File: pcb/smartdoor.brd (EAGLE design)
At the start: 40.3 x 53.3 mm, 5 parts

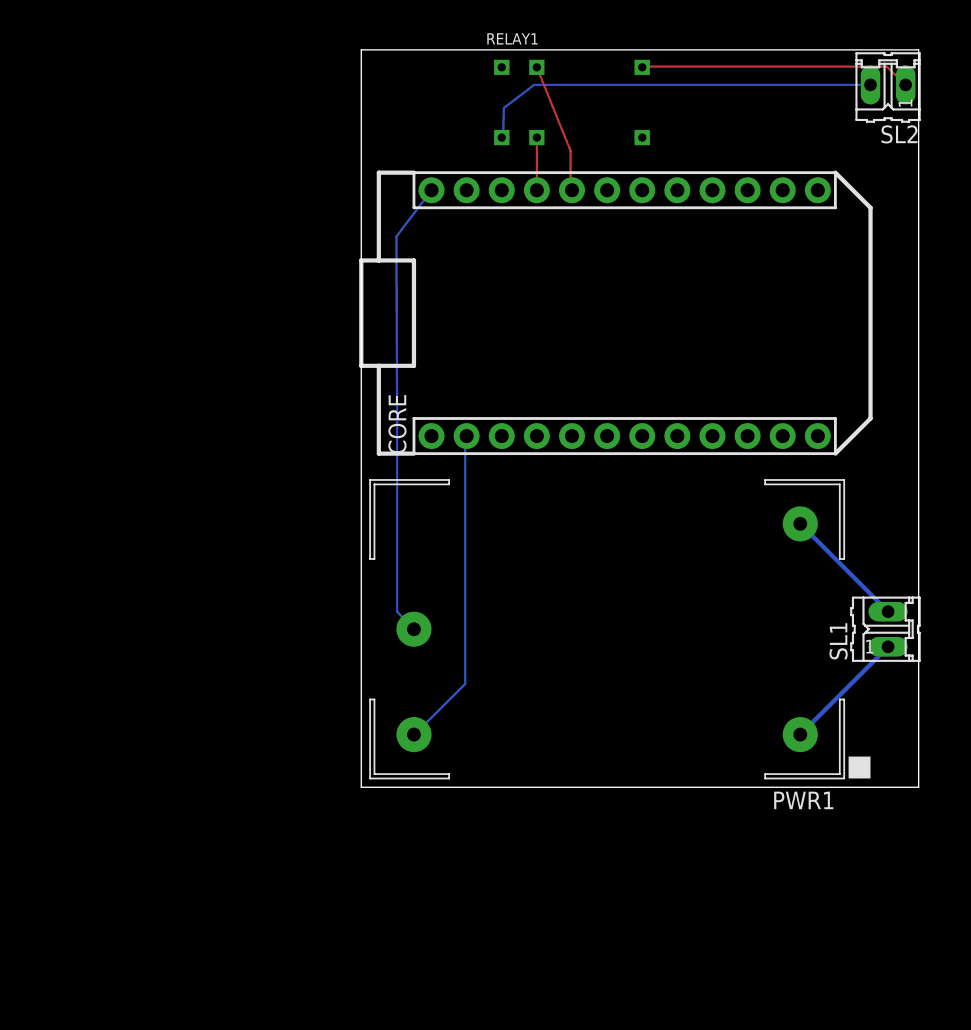
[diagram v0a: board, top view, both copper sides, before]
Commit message: new pcb board layout, renamed files
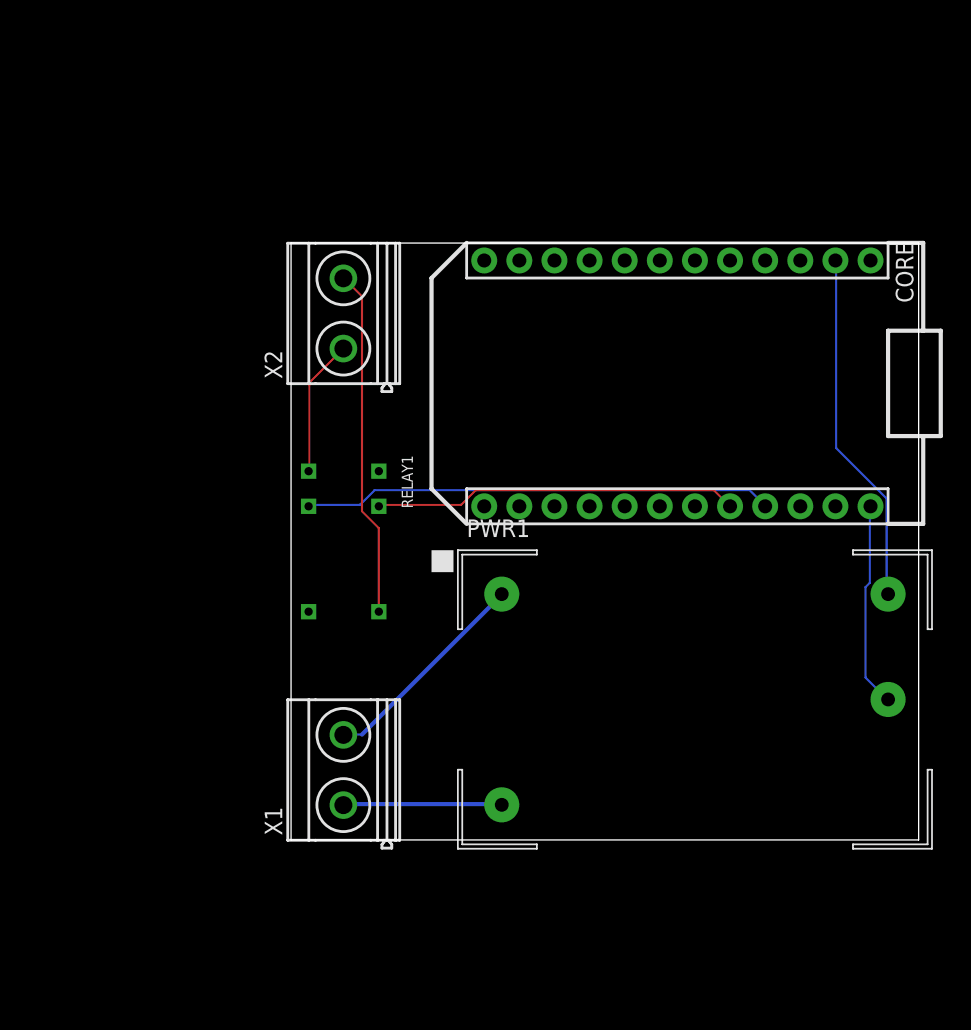
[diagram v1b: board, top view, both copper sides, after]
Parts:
- removed SL1, SL2: (no value), con-amp-quick:02P
- added X1, X2: MKDSN1,5/2-5,08, con-phoenix-508:MKDSN1,5/2-5,08
- moved RELAY1 35.8 mm to (20.3, 33.0), turned to 270 degrees
- moved PWR1 6.35 mm to (44.5, 21.6), turned to 0 degrees
- moved CORE 6.35 mm to (44.5, 44.5), turned to 270 degrees
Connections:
- net L: now also X1.1; no longer SL1.2
- net LOAD+: now also X2.2; no longer SL2.1
- net LOAD-: now also X2.1; no longer SL2.2
- net N: now also X1.2; no longer SL1.1
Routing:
- net GND2: track 3.81 -> 34.0 mm
- net LOAD-: track 29.3 -> 9.94 mm
- net 3V3: track 33.1 -> 14.8 mm
- net SWITCH: track 9.41 -> 26.4 mm
- net N: track 8.98 -> 15.7 mm
- net LOAD+: track 19.6 -> 25.2 mm
- net GND: track 23.2 -> 25.8 mm
- net L: track 8.98 -> 11.5 mm
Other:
- board size 40.3 x 53.3 mm -> 45.4 x 43.2 mm

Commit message: defined net classes and GND pins on relay, new board layout
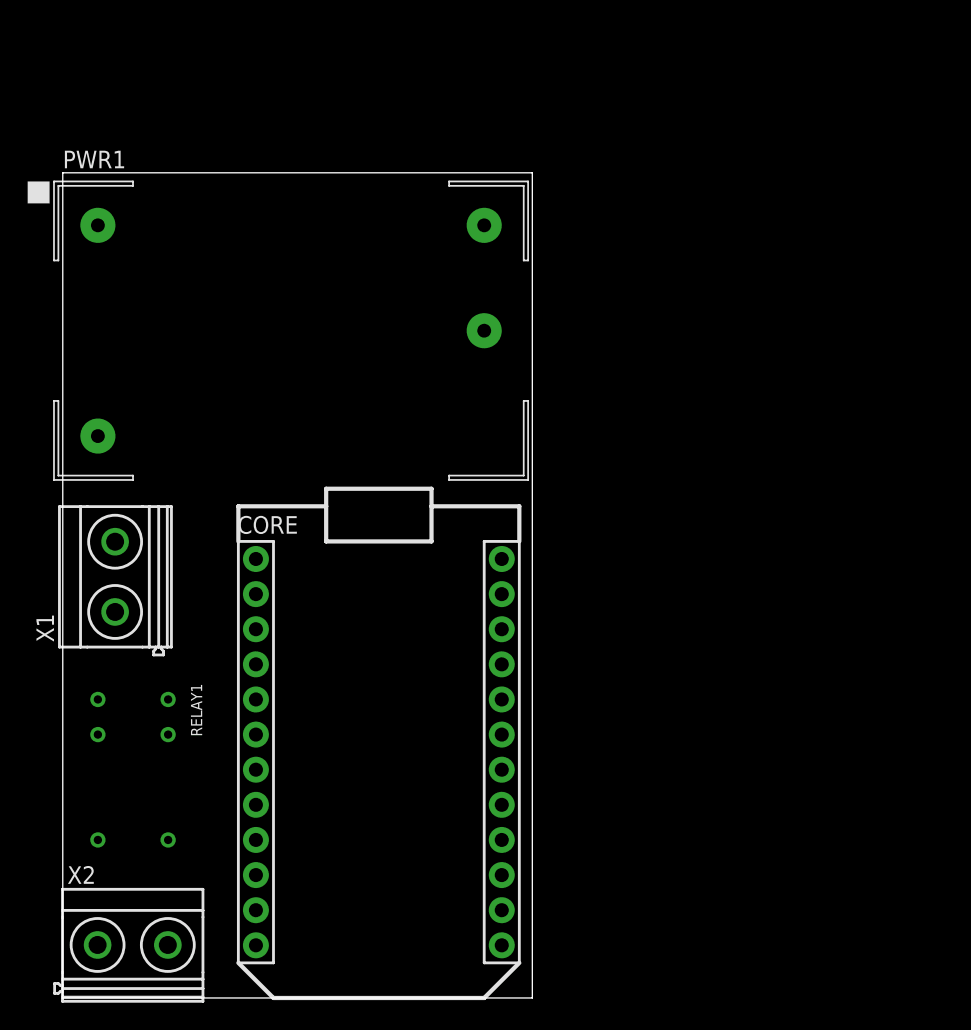
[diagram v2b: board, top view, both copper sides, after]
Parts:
- moved X2 48.2 mm to (5.08, 3.81), turned to 0 degrees
- moved PWR1 39.6 mm to (15.2, 48.3)
- moved CORE 34.3 mm to (22.9, 17.8), turned to 0 degrees
- moved RELAY1 22.5 mm to (5.08, 16.5)
- moved X1 21.6 mm to (3.81, 30.5)
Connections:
- removed net GND2: CORE.21, RELAY1.9
- new net N$1: CORE.2, PWR1.P3
- net GND: now also CORE.21, RELAY1.9; no longer CORE.2, PWR1.P3
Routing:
- net GND2: track 34.0 -> 0.00 mm
- net SWITCH: track 26.4 -> 0.00 mm
- net GND: track 25.8 -> 0.00 mm
- net LOAD+: track 25.2 -> 0.00 mm
- net N: track 15.7 -> 0.00 mm
- net 3V3: track 14.8 -> 0.00 mm
- net L: track 11.5 -> 0.00 mm
- net LOAD-: track 9.94 -> 0.00 mm
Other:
- board size 45.4 x 43.2 mm -> 34 x 59.7 mm
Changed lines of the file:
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@@
 <board>
 <plain>
-<wire x1="16.51" y1="11.43" x2="61.9" y2="11.43" width="0" layer="20"/>
-<wire x1="61.9" y1="11.43" x2="61.9" y2="54.6" width="0" layer="20"/>
-<wire x1="61.9" y1="54.6" x2="16.51" y2="54.6" width="0" layer="20"/>
-<wire x1="16.51" y1="54.6" x2="16.51" y2="11.43" width="0" layer="20"/>
+<wire x1="0" y1="0" x2="33.96" y2="0" width="0" layer="20"/>
+<wire x1="33.96" y1="0" x2="33.96" y2="59.68" width="0" layer="20"/>
+<wire x1="33.96" y1="59.68" x2="0" y2="59.68" width="0" layer="20"/>
+<wire x1="0" y1="59.68" x2="0" y2="0" width="0" layer="20"/>
 </plain>
 <attributes>
@@
 </variantdefs>
 <classes>
-<class number="0" name="default" width="0" drill="0">
+<class number="0" name="default" width="0.6096" drill="0.6096">
+<clearance class="0" value="0.6096"/>
 </class>
 </classes>
@@
 <param name="RoutingGrid" value="50mil"/>
 <param name="AutoGrid" value="1"/>
-<param name="Efforts" value="2"/>
+<param name="Efforts" value="0"/>
 <param name="TopRouterVariant" value="1"/>
 <param name="tpViaShape" value="round"/>
@@
 </autorouter>
 <elements>
-<element name="CORE" library="Particle" package="SPARK_CORE" value="SPARK_CORECORE" x="44.45" y="44.45" rot="R270"/>
-<element name="PWR1" library="recom-powerline-acdc-converters" package="LOW_PROFILE_POWER_MODULE" value="RAC02-3.3SC" x="44.45" y="21.59">
-<attribute name="INPUT_RANGE" value="80 - 277 (VAC)" x="44.45" y="21.59" size="1.778" layer="27" display="off"/>
-<attribute name="MAX_CAPACITIVE_LOAD" value="2000uF" x="44.45" y="21.59" size="1.778" layer="27" display="off"/>
-<attribute name="OUTPUT_CURRENT" value="600mA" x="44.45" y="21.59" size="1.778" layer="27" display="off"/>
-<attribute name="OUTPUT_VOLTAGE" value="3.3v" x="44.45" y="21.59" size="1.778" layer="27" display="off"/>
+<element name="CORE" library="Particle" package="SPARK_CORE" value="SPARK_CORECORE" x="22.86" y="17.78"/>
+<element name="PWR1" library="recom-powerline-acdc-converters" package="LOW_PROFILE_POWER_MODULE" value="RAC02-3.3SC" x="15.24" y="48.26">
+<attribute name="INPUT_RANGE" value="80 - 277 (VAC)" x="15.24" y="48.26" size="1.778" layer="27" display="off"/>
+<attribute name="MAX_CAPACITIVE_LOAD" value="2000uF" x="15.24" y="48.26" size="1.778" layer="27" display="off"/>
+<attribute name="OUTPUT_CURRENT" value="600mA" x="15.24" y="48.26" size="1.778" layer="27" display="off"/>
+<attribute name="OUTPUT_VOLTAGE" value="3.3v" x="15.24" y="48.26" size="1.778" layer="27" display="off"/>
 </element>
-<element name="RELAY1" library="Zettler" package="AZ9571" value="AZ9571AZ9571" x="20.32" y="33.02" rot="R270"/>
-<element name="X1" library="con-phoenix-508" library_urn="urn:adsk.eagle:library:176" package="MKDSN1,5/2-5,08" value="MKDSN1,5/2-5,08" x="20.32" y="16.51" rot="R90"/>
-<element name="X2" library="con-phoenix-508" library_urn="urn:adsk.eagle:library:176" package="MKDSN1,5/2-5,08" value="MKDSN1,5/2-5,08" x="20.32" y="49.53" rot="R90"/>
+<element name="RELAY1" library="Zettler" package="AZ9571" value="AZ9571AZ9571" x="5.08" y="16.51" rot="R270"/>
+<element name="X1" library="con-phoenix-508" library_urn="urn:adsk.eagle:library:176" package="MKDSN1,5/2-5,08" value="MKDSN1,5/2-5,08" x="3.81" y="30.48" rot="R90"/>
+<element name="X2" library="con-phoenix-508" library_urn="urn:adsk.eagle:library:176" package="MKDSN1,5/2-5,08" value="MKDSN1,5/2-5,08" x="5.08" y="3.81"/>
 </elements>
 <signals>
@@
 <contactref element="CORE" pad="22"/>
 </signal>
+<signal name="GND">
+<contactref element="CORE" pad="21"/>
+<contactref element="RELAY1" pad="9"/>
+<wire x1="31.75" y1="24.13" x2="2.54" y2="19.05" width="0" layer="19" extent="1-1"/>
+</signal>
 <signal name="N">
 <contactref element="PWR1" pad="P1"/>
 <contactref element="X1" pad="2"/>
-<wire x1="21.6408" y1="19.05" x2="20.4216" y2="19.05" width="0.1524" layer="16"/>
-<wire x1="31.6992" y1="29.1084" x2="21.6408" y2="19.05" width="0.3048" layer="16"/>
-<wire x1="20.4216" y1="19.05" x2="20.295" y2="19.0289" width="0.1524" layer="16"/>
-<wire x1="31.6992" y1="29.1084" x2="31.75" y2="29.21" width="0.1524" layer="16"/>
+<wire x1="2.54" y1="55.88" x2="3.785" y2="32.9989" width="0" layer="19" extent="1-1"/>
 </signal>
 <signal name="L">
 <contactref element="PWR1" pad="P2"/>
 <contactref element="X1" pad="1"/>
-<wire x1="31.6992" y1="14.0208" x2="20.4216" y2="14.0208" width="0.3048" layer="16"/>
-<wire x1="20.4216" y1="14.0208" x2="20.295" y2="13.9489" width="0.1524" layer="16"/>
-<wire x1="31.6992" y1="14.0208" x2="31.75" y2="13.97" width="0.1524" layer="16"/>
+<wire x1="2.54" y1="40.64" x2="3.785" y2="27.9189" width="0" layer="19" extent="1-1"/>
 </signal>
 <signal name="3V3">
 <contactref element="PWR1" pad="P4"/>
 <contactref element="CORE" pad="24"/>
-<wire x1="58.3692" y1="30.0228" x2="58.3692" y2="35.5092" width="0.1524" layer="16"/>
-<wire x1="58.0644" y1="29.718" x2="58.3692" y2="30.0228" width="0.1524" layer="16"/>
-<wire x1="58.0644" y1="23.1648" x2="58.0644" y2="29.718" width="0.1524" layer="16"/>
-<wire x1="59.5884" y1="21.6408" x2="58.0644" y2="23.1648" width="0.1524" layer="16"/>
-<wire x1="58.3692" y1="35.5092" x2="58.42" y2="35.56" width="0.1524" layer="16"/>
-<wire x1="59.5884" y1="21.6408" x2="59.69" y2="21.59" width="0.1524" layer="16"/>
-</signal>
-<signal name="GND">
-<contactref element="PWR1" pad="P3"/>
-<contactref element="CORE" pad="2"/>
-<wire x1="55.9308" y1="39.7764" x2="55.9308" y2="53.34" width="0.1524" layer="16"/>
-<wire x1="59.5884" y1="36.1188" x2="55.9308" y2="39.7764" width="0.1524" layer="16"/>
-<wire x1="59.5884" y1="29.2608" x2="59.5884" y2="36.1188" width="0.1524" layer="16"/>
-<wire x1="55.9308" y1="53.34" x2="55.88" y2="53.34" width="0.1524" layer="16"/>
-<wire x1="59.5884" y1="29.2608" x2="59.69" y2="29.21" width="0.1524" layer="16"/>
+<wire x1="31.75" y1="31.75" x2="30.48" y2="48.26" width="0" layer="19" extent="1-1"/>
 </signal>
 <signal name="LOAD+">
 <contactref element="RELAY1" pad="6"/>
 <contactref element="X2" pad="2"/>
-<wire x1="22.86" y1="33.9852" x2="22.86" y2="27.94" width="0.1524" layer="1"/>
-<wire x1="21.6408" y1="35.2044" x2="22.86" y2="33.9852" width="0.1524" layer="1"/>
-<wire x1="21.6408" y1="50.7492" x2="21.6408" y2="35.2044" width="0.1524" layer="1"/>
-<wire x1="20.4216" y1="51.9684" x2="21.6408" y2="50.7492" width="0.1524" layer="1"/>
-<wire x1="20.4216" y1="51.9684" x2="20.295" y2="52.0489" width="0.1524" layer="1"/>
+<wire x1="7.62" y1="11.43" x2="7.5989" y2="3.835" width="0" layer="19" extent="1-1"/>
 </signal>
 <signal name="LOAD-">
 <contactref element="RELAY1" pad="1"/>
 <contactref element="X2" pad="1"/>
-<wire x1="17.8308" y1="44.5008" x2="17.8308" y2="38.1" width="0.1524" layer="1"/>
-<wire x1="20.2692" y1="46.9392" x2="17.8308" y2="44.5008" width="0.1524" layer="1"/>
-<wire x1="17.8308" y1="38.1" x2="17.78" y2="38.1" width="0.1524" layer="1"/>
-<wire x1="20.2692" y1="46.9392" x2="20.295" y2="46.9689" width="0.1524" layer="1"/>
-</signal>
-<signal name="GND2">
-<contactref element="RELAY1" pad="9"/>
-<contactref element="CORE" pad="21"/>
-<wire x1="21.4884" y1="35.6616" x2="17.8308" y2="35.6616" width="0.1524" layer="16"/>
-<wire x1="22.5552" y1="36.7284" x2="21.4884" y2="35.6616" width="0.1524" layer="16"/>
-<wire x1="49.6824" y1="36.7284" x2="22.5552" y2="36.7284" width="0.1524" layer="16"/>
-<wire x1="50.7492" y1="35.6616" x2="49.6824" y2="36.7284" width="0.1524" layer="16"/>
-<wire x1="17.8308" y1="35.6616" x2="17.78" y2="35.56" width="0.1524" layer="16"/>
-<wire x1="50.7492" y1="35.6616" x2="50.8" y2="35.56" width="0.1524" layer="16"/>
+<wire x1="2.54" y1="21.59" x2="2.5189" y2="3.835" width="0" layer="19" extent="1-1"/>
 </signal>
 <signal name="SWITCH">
 <contactref element="CORE" pad="20"/>
 <contactref element="RELAY1" pad="2"/>
-<wire x1="28.8036" y1="35.6616" x2="22.86" y2="35.6616" width="0.1524" layer="1"/>
-<wire x1="29.8704" y1="36.7284" x2="28.8036" y2="35.6616" width="0.1524" layer="1"/>
-<wire x1="47.0916" y1="36.7284" x2="29.8704" y2="36.7284" width="0.1524" layer="1"/>
-<wire x1="48.26" y1="35.56" x2="47.0916" y2="36.7284" width="0.1524" layer="1"/>
-<wire x1="22.86" y1="35.6616" x2="22.86" y2="35.56" width="0.1524" layer="1"/>
+<wire x1="31.75" y1="21.59" x2="7.62" y2="19.05" width="0" layer="19" extent="1-1"/>
+</signal>
+<signal name="N$1">
+<contactref element="PWR1" pad="P3"/>
+<contactref element="CORE" pad="2"/>
+<wire x1="13.97" y1="29.21" x2="30.48" y2="55.88" width="0" layer="19" extent="1-1"/>
 </signal>
 </signals>

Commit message: final board with two net classes, ground fills and non-via routings
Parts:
- turned X1 to 270 degrees
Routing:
- net SWITCH: track 0.00 -> 44.4 mm
- net N$1: track 0.00 -> 41.3 mm
- net N: track 0.00 -> 33.8 mm
- net LOAD-: track 0.00 -> 21.3 mm
- net 3V3: track 0.00 -> 17.6 mm
- net L: track 0.00 -> 8.13 mm
- net LOAD+: track 0.00 -> 7.60 mm
- added copper zone on layer 1, net GND
- added copper zone on layer 16, net GND
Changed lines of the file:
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@@
 <clearance class="0" value="0.6096"/>
+</class>
+<class number="1" name="hivoltage" width="1.016" drill="0.6096">
+<clearance class="1" value="1.016"/>
 </class>
 </classes>
@@
 <param name="RoutingGrid" value="50mil"/>
 <param name="AutoGrid" value="1"/>
-<param name="Efforts" value="0"/>
+<param name="Efforts" value="2"/>
 <param name="TopRouterVariant" value="1"/>
 <param name="tpViaShape" value="round"/>
@@
 </element>
 <element name="RELAY1" library="Zettler" package="AZ9571" value="AZ9571AZ9571" x="5.08" y="16.51" rot="R270"/>
-<element name="X1" library="con-phoenix-508" library_urn="urn:adsk.eagle:library:176" package="MKDSN1,5/2-5,08" value="MKDSN1,5/2-5,08" x="3.81" y="30.48" rot="R90"/>
+<element name="X1" library="con-phoenix-508" library_urn="urn:adsk.eagle:library:176" package="MKDSN1,5/2-5,08" value="MKDSN1,5/2-5,08" x="3.81" y="30.48" rot="R270"/>
 <element name="X2" library="con-phoenix-508" library_urn="urn:adsk.eagle:library:176" package="MKDSN1,5/2-5,08" value="MKDSN1,5/2-5,08" x="5.08" y="3.81"/>
 </elements>
@@
 <contactref element="CORE" pad="21"/>
 <contactref element="RELAY1" pad="9"/>
-<wire x1="31.75" y1="24.13" x2="2.54" y2="19.05" width="0" layer="19" extent="1-1"/>
-</signal>
-<signal name="N">
+<polygon width="0.254" layer="16" isolate="0.4064">
+<vertex x="0" y="0"/>
+<vertex x="34.29" y="0"/>
+<vertex x="34.29" y="59.69"/>
+<vertex x="0" y="59.69"/>
+</polygon>
+<polygon width="0.254" layer="1" isolate="0.4064">
+<vertex x="0" y="0"/>
+<vertex x="34.29" y="0"/>
+<vertex x="34.29" y="59.69"/>
+<vertex x="0" y="59.69"/>
+</polygon>
+</signal>
+<signal name="N" class="1">
 <contactref element="PWR1" pad="P1"/>
 <contactref element="X1" pad="2"/>
-<wire x1="2.54" y1="55.88" x2="3.785" y2="32.9989" width="0" layer="19" extent="1-1"/>
-</signal>
-<signal name="L">
+<wire x1="7.62" y1="28.575" x2="4.445" y2="28.575" width="1.016" layer="16"/>
+<wire x1="7.62" y1="50.8" x2="7.62" y2="28.575" width="1.016" layer="16"/>
+<wire x1="3.175" y1="55.245" x2="7.62" y2="50.8" width="1.016" layer="16"/>
+<wire x1="2.54" y1="55.245" x2="3.175" y2="55.245" width="1.016" layer="16"/>
+<wire x1="2.54" y1="55.88" x2="2.54" y2="55.245" width="1.016" layer="16"/>
+<wire x1="4.445" y1="28.575" x2="3.835" y2="27.9611" width="1.016" layer="16"/>
+</signal>
+<signal name="L" class="1">
 <contactref element="PWR1" pad="P2"/>
 <contactref element="X1" pad="1"/>
-<wire x1="2.54" y1="40.64" x2="3.785" y2="27.9189" width="0" layer="19" extent="1-1"/>
+<wire x1="3.175" y1="34.29" x2="3.81" y2="33.655" width="1.016" layer="16"/>
+<wire x1="3.175" y1="39.37" x2="3.175" y2="34.29" width="1.016" layer="16"/>
+<wire x1="2.54" y1="40.005" x2="3.175" y2="39.37" width="1.016" layer="16"/>
+<wire x1="2.54" y1="40.64" x2="2.54" y2="40.005" width="1.016" layer="16"/>
+<wire x1="3.81" y1="33.655" x2="3.835" y2="33.0411" width="1.016" layer="16"/>
 </signal>
 <signal name="3V3">
 <contactref element="PWR1" pad="P4"/>
 <contactref element="CORE" pad="24"/>
-<wire x1="31.75" y1="31.75" x2="30.48" y2="48.26" width="0" layer="19" extent="1-1"/>
+<wire x1="29.845" y1="33.655" x2="31.75" y2="31.75" width="0.6096" layer="16"/>
+<wire x1="29.845" y1="47.625" x2="29.845" y2="33.655" width="0.6096" layer="16"/>
+<wire x1="30.48" y1="48.26" x2="29.845" y2="47.625" width="0.6096" layer="16"/>
 </signal>
 <signal name="LOAD+">
 <contactref element="RELAY1" pad="6"/>
 <contactref element="X2" pad="2"/>
-<wire x1="7.62" y1="11.43" x2="7.5989" y2="3.835" width="0" layer="19" extent="1-1"/>
+<wire x1="7.62" y1="4.445" x2="7.62" y2="11.43" width="0.6096" layer="16"/>
+<wire x1="7.62" y1="4.445" x2="7.5989" y2="3.835" width="0.6096" layer="16"/>
 </signal>
 <signal name="LOAD-">
 <contactref element="RELAY1" pad="1"/>
 <contactref element="X2" pad="1"/>
-<wire x1="2.54" y1="21.59" x2="2.5189" y2="3.835" width="0" layer="19" extent="1-1"/>
+<wire x1="5.08" y1="21.59" x2="2.54" y2="21.59" width="0.6096" layer="16"/>
+<wire x1="5.08" y1="6.985" x2="5.08" y2="21.59" width="0.6096" layer="16"/>
+<wire x1="2.54" y1="4.445" x2="5.08" y2="6.985" width="0.6096" layer="16"/>
+<wire x1="2.54" y1="4.445" x2="2.5189" y2="3.835" width="0.6096" layer="16"/>
 </signal>
 <signal name="SWITCH">
 <contactref element="CORE" pad="20"/>
 <contactref element="RELAY1" pad="2"/>
-<wire x1="31.75" y1="21.59" x2="7.62" y2="19.05" width="0" layer="19" extent="1-1"/>
+<wire x1="8.89" y1="19.05" x2="7.62" y2="19.05" width="0.6096" layer="1"/>
+<wire x1="10.795" y1="20.955" x2="8.89" y2="19.05" width="0.6096" layer="1"/>
+<wire x1="10.795" y1="34.925" x2="10.795" y2="20.955" width="0.6096" layer="1"/>
+<wire x1="17.145" y1="34.925" x2="10.795" y2="34.925" width="0.6096" layer="1"/>
+<wire x1="30.48" y1="21.59" x2="17.145" y2="34.925" width="0.6096" layer="1"/>
+<wire x1="31.75" y1="21.59" x2="30.48" y2="21.59" width="0.6096" layer="1"/>
 </signal>
 <signal name="N$1">
 <contactref element="PWR1" pad="P3"/>
 <contactref element="CORE" pad="2"/>
-<wire x1="13.97" y1="29.21" x2="30.48" y2="55.88" width="0" layer="19" extent="1-1"/>
+<wire x1="27.305" y1="29.21" x2="13.97" y2="29.21" width="0.6096" layer="16"/>
+<wire x1="27.305" y1="52.705" x2="27.305" y2="29.21" width="0.6096" layer="16"/>
+<wire x1="30.48" y1="55.88" x2="27.305" y2="52.705" width="0.6096" layer="16"/>
 </signal>
 </signals>
